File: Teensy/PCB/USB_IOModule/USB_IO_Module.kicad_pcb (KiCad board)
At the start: 2 copper layers, 55.9 x 106.7 mm, 101 parts, among them J1 USB_B, J2 USB_A, J3 Power_Connector_2x3, U1 SC16IS762IPW, U2 Teensy4.0, X1 XO53

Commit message: Generated Gerbers
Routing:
- net /T21: track 36.2 -> 38.0 mm
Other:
- board text added: "+"

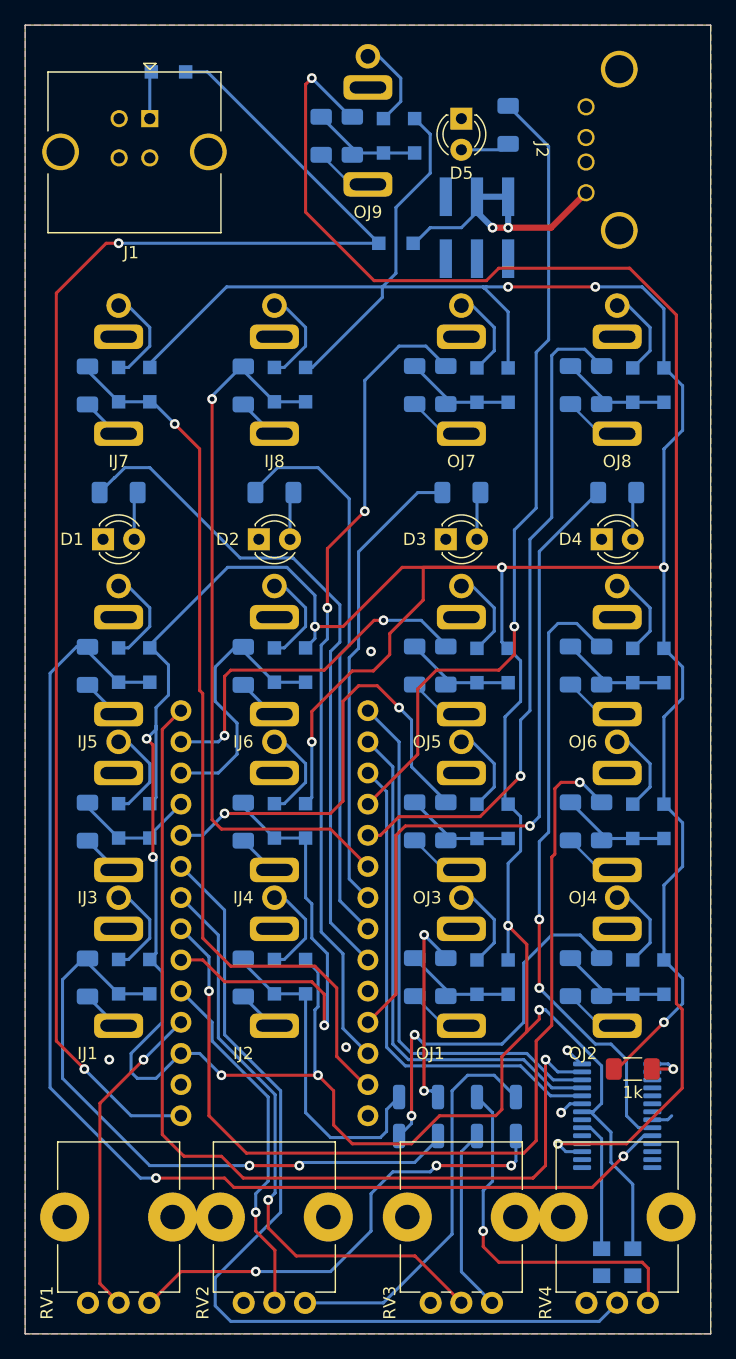
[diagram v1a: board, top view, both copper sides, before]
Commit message: Made NPTH holes 0.5mm bigger; adjusted diode pads for better solderability
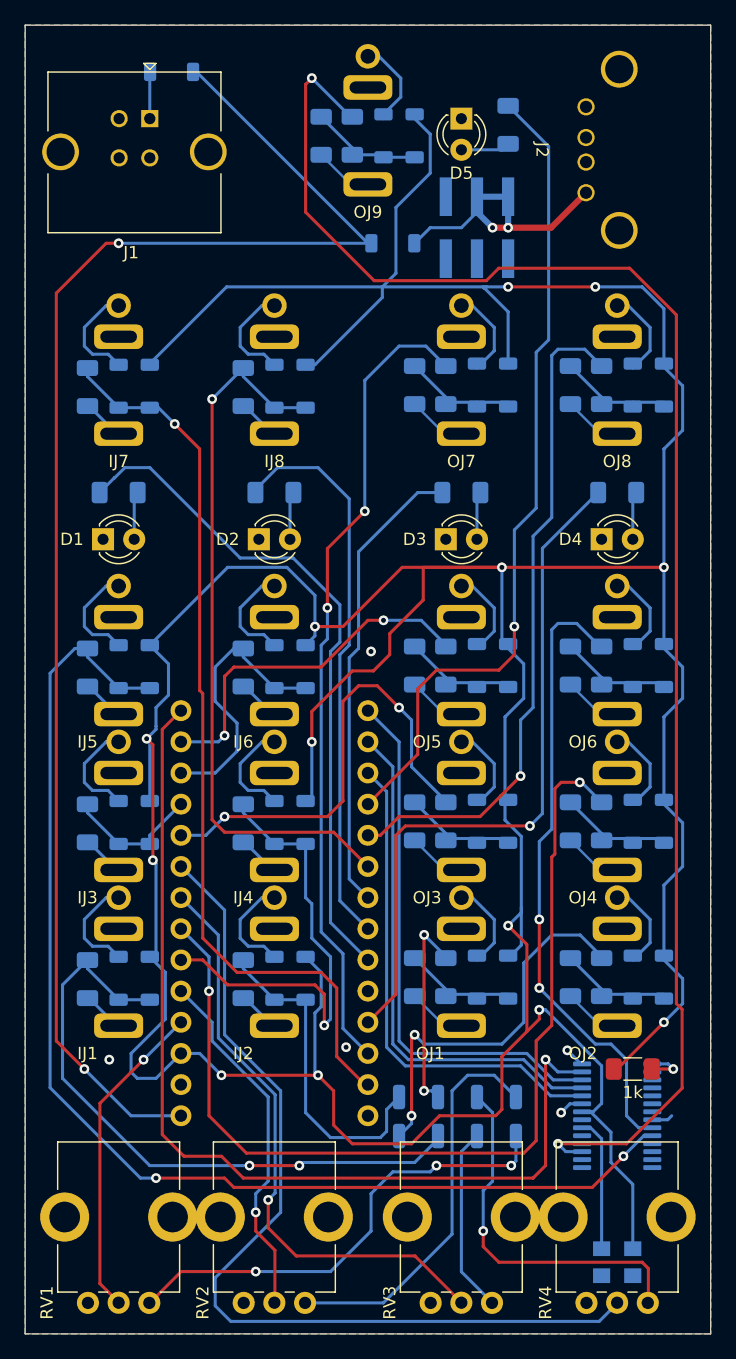
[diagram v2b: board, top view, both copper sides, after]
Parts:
- D6, D7, ID1, ID10, ID11, ID12, ID13, ID14, ID15, ID16, ID2, ID3, ID4, ID5, ID6, ID7, ID8, ID9, OD1, OD10, OD11, OD12, OD13, OD14, OD15, OD16, OD17, OD18, OD2, OD3, OD4, OD5, OD6, OD7, OD8, OD9: footprint Diode_SMD:D_SOD-123F -> Misc:D_SOD-123 Handsolder
- moved D7 0.25 mm to (118.9, 81.3)
- moved D6 0.25 mm to (100.8, 67.3)
- moved ID1 0.13 mm to (96.5, 141.2)
- moved ID2 0.13 mm to (99.1, 141.2)
- moved ID3 0.13 mm to (109.2, 141.2)
- moved ID4 0.13 mm to (111.8, 141.2)
- moved ID10 0.13 mm to (99.1, 115.8)
- moved ID11 0.13 mm to (109.2, 115.8)
- moved ID12 0.13 mm to (111.8, 115.8)
- moved ID13 0.13 mm to (96.5, 92.9)
- moved ID14 0.13 mm to (99.1, 92.9)
- moved ID15 0.13 mm to (109.2, 92.9)
- moved ID16 0.13 mm to (111.8, 92.9)
- moved ID9 0.13 mm to (96.5, 115.8)
- moved ID5 0.13 mm to (96.5, 128.5)
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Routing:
- net GND: track 135.6 -> 138.6 mm
- net +5V: track 123.1 -> 121.3 mm
- net +3.3V: track 399.9 -> 401.2 mm
- net /T16: track 10.3 -> 11.1 mm
